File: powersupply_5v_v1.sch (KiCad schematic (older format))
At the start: 38 parts, among them P1 AC_INPUT, P2 POWER OUT, T1 TRANSFO2, U1 LM7805CT/NOPB

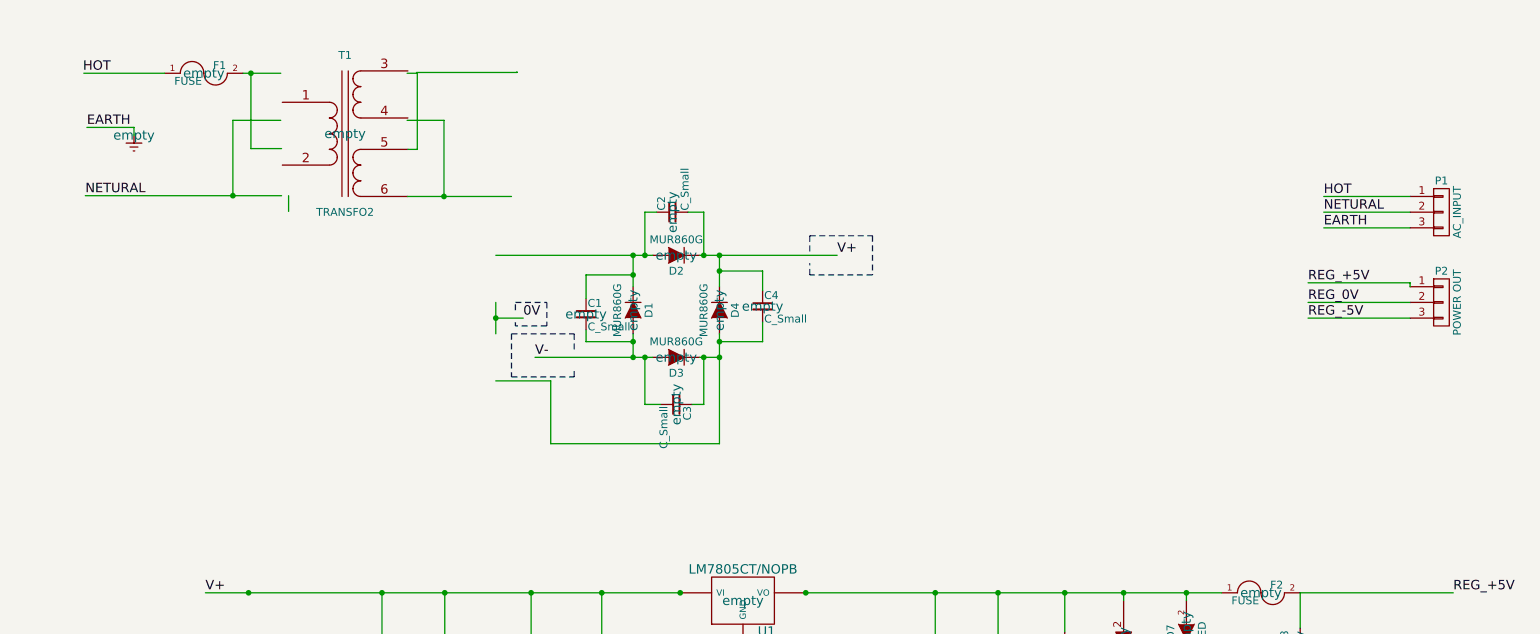
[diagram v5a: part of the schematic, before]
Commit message: added a small circuit for showing a LED indication when AC power is live
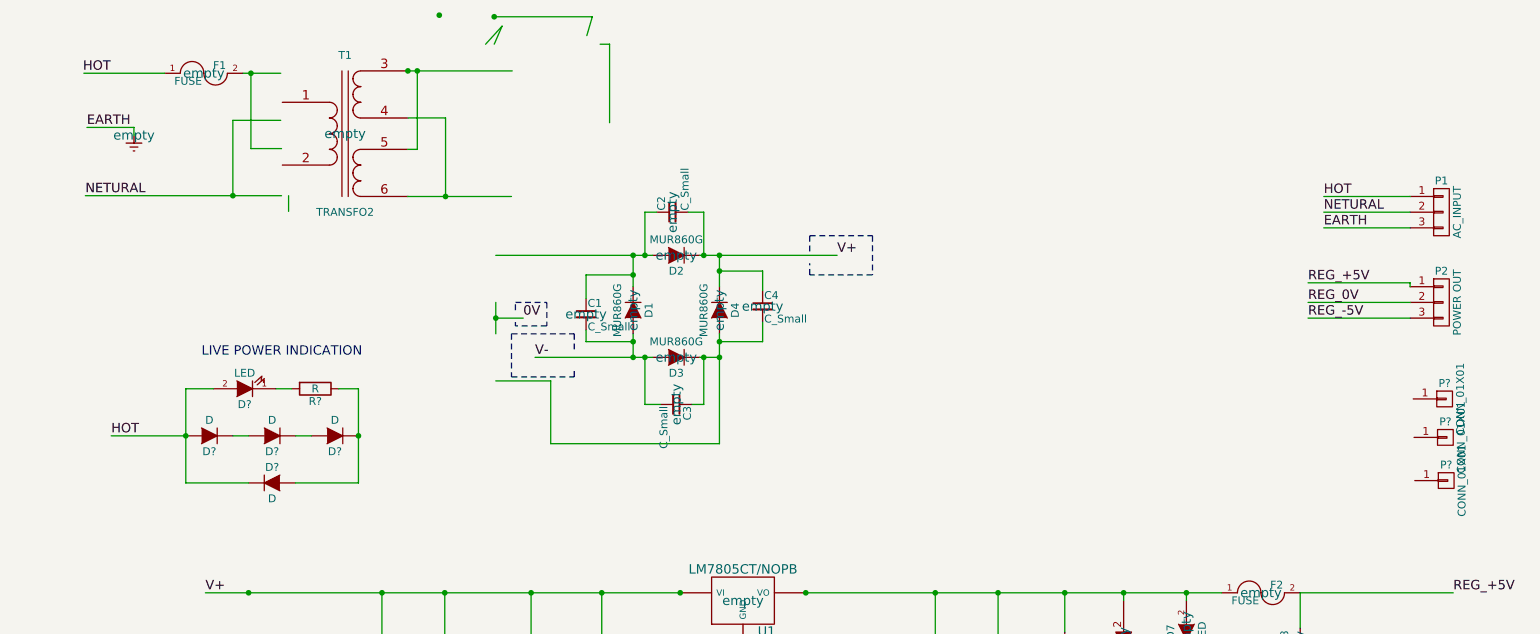
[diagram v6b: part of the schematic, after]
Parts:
- added D? (x4): D, symbol D
- added D?: LED, symbol LED
- added P? (x3): CONN_01X01, symbol CONN_01X01
- added R?: R, symbol R
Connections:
- wire segments 96 -> 110
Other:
- note added: "LIVE POWER INDICATION"
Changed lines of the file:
@@
 	1600 5255 1615 5255
 Wire Wire Line
-	2710 1240 2775 1240
+	2710 1225 3380 1225
 Wire Wire Line
-	2775 1240 2775 1725
+	3940 1055 4000 1055
 Wire Wire Line
-	2945 1540 2945 2025
+	4000 1055 4000 1555
+Wire Wire Line
+	2955 1525 2955 2025
 Wire Wire Line
 	2715 2025 3375 2025
@@
 Connection ~ 1600 2020
 Wire Wire Line
-	2710 1540 2945 1540
+	2715 1525 2955 1525
 Wire Wire Line
 	2775 1725 2715 1725
-Connection ~ 2945 2025
+Connection ~ 2955 2025
 Wire Wire Line
-	2770 1235 3410 1235
+	3265 1055 3315 940
 Wire Wire Line
-	3410 1235 3410 1230
+	3265 880  3890 880
+Wire Wire Line
+	3890 880  3855 1000
+Wire Wire Line
+	3315 940  3210 1055
+Connection ~ 2915 870
+Connection ~ 3265 880
+Wire Wire Line
+	2775 1225 2775 1725
+Connection ~ 2715 1225
+Connection ~ 2775 1225
+$Comp
+L CONN_01X01 P?
+U 1 1 563D69E3
+P 9320 3315
+F 0 "P?" H 9320 3415 50  0000 C CNN
+F 1 "CONN_01X01" V 9420 3315 50  0000 C CNN
+F 2 "" H 9320 3315 60  0000 C CNN
+F 3 "" H 9320 3315 60  0000 C CNN
+	1    9320 3315
+	1    0    0    -1
+$EndComp
+$Comp
+L CONN_01X01 P?
+U 1 1 563D6B9B
+P 9330 3835
+F 0 "P?" H 9330 3935 50  0000 C CNN
+F 1 "CONN_01X01" V 9430 3835 50  0000 C CNN
+F 2 "" H 9330 3835 60  0000 C CNN
+F 3 "" H 9330 3835 60  0000 C CNN
+	1    9330 3835
+	1    0    0    -1
+$EndComp
+$Comp
+L CONN_01X01 P?
+U 1 1 563D6D87
+P 9325 3560
+F 0 "P?" H 9325 3660 50  0000 C CNN
+F 1 "CONN_01X01" V 9425 3560 50  0000 C CNN
+F 2 "" H 9325 3560 60  0000 C CNN
+F 3 "" H 9325 3560 60  0000 C CNN
+	1    9325 3560
+	1    0    0    -1
+$EndComp
+$Comp
+L D D?
+U 1 1 563D8C84
+P 1450 3550
+F 0 "D?" H 1450 3650 50  0000 C CNN
+F 1 "D" H 1450 3450 50  0000 C CNN
+F 2 "" H 1450 3550 60  0000 C CNN
+F 3 "" H 1450 3550 60  0000 C CNN
+	1    1450 3550
+	-1   0    0    1
+$EndComp
+$Comp
+L D D?
+U 1 1 563D8D7D
+P 1850 3550
+F 0 "D?" H 1850 3650 50  0000 C CNN
+F 1 "D" H 1850 3450 50  0000 C CNN
+F 2 "" H 1850 3550 60  0000 C CNN
+F 3 "" H 1850 3550 60  0000 C CNN
+	1    1850 3550
+	-1   0    0    1
+$EndComp
+$Comp
+L D D?
+U 1 1 563D8E34
+P 2250 3550
+F 0 "D?" H 2250 3650 50  0000 C CNN
+F 1 "D" H 2250 3450 50  0000 C CNN
+F 2 "" H 2250 3550 60  0000 C CNN
+F 3 "" H 2250 3550 60  0000 C CNN
+	1    2250 3550
+	-1   0    0    1
+$EndComp
+$Comp
+L D D?
+U 1 1 563D8EE4
+P 1850 3850
+F 0 "D?" H 1850 3950 50  0000 C CNN
+F 1 "D" H 1850 3750 50  0000 C CNN
+F 2 "" H 1850 3850 60  0000 C CNN
+F 3 "" H 1850 3850 60  0000 C CNN
+	1    1850 3850
+	1    0    0    -1
+$EndComp
+Wire Wire Line
+	1600 3550 1700 3550
+Wire Wire Line
+	2000 3550 2100 3550
+Wire Wire Line
+	2400 3250 2400 3850
+Wire Wire Line
+	2400 3850 2000 3850
+Wire Wire Line
+	1300 3850 1700 3850
+Wire Wire Line
+	1300 3250 1300 3850
+$Comp
+L R R?
+U 1 1 563D9406
+P 2125 3250
+F 0 "R?" V 2205 3250 50  0000 C CNN
+F 1 "R" V 2125 3250 50  0000 C CNN
+F 2 "" V 2055 3250 30  0000 C CNN
+F 3 "" H 2125 3250 30  0000 C CNN
+	1    2125 3250
+	0    1    1    0
+$EndComp
+$Comp
+L LED D?
+U 1 1 563D94D3
+P 1675 3250
+F 0 "D?" H 1675 3350 50  0000 C CNN
+F 1 "LED" H 1675 3150 50  0000 C CNN
+F 2 "" H 1675 3250 60  0000 C CNN
+F 3 "" H 1675 3250 60  0000 C CNN
+	1    1675 3250
+	-1   0    0    1
+$EndComp
+Wire Wire Line
+	2275 3250 2400 3250
+Connection ~ 2400 3550
+Wire Wire Line
+	1975 3250 1875 3250
+Wire Wire Line
+	1475 3250 1300 3250
+Connection ~ 1300 3550
+Text Label 825  3550 0    60   ~ 0
+HOT
+Wire Wire Line
+	825  3550 1300 3550
+Text Notes 1400 3050 0    60   ~ 0
+LIVE POWER INDICATION
 $EndSCHEMATC
